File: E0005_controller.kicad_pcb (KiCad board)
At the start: 4 copper layers, 125 x 73 mm, 270 parts, among them J1 SM04B-GHS-TB, J10 FH12-18S-0.5SH, J11 USB4105-GF-A, J12 SM02B-GHS-TB, J2 SM04B-GHS-TB, J3 SM04B-GHS-TB, J4 SM04B-GHS-TB, J5 SM06B-GHS-TB, J6 SM02B-GHS-TB, J7 SM02B-GHS-TB, J8 SM02B-GHS-TB, J9 SM02B-GHS-TB, Q1 PSMN2R0-30YLDX, Q11 2N7002, Q12 2N7002, Q13 AO3401A, Q14 2N7002, Q2 PSMN2R0-30YLDX, Q3 2N7002, Q4 2N7002, Q5 2N7002, Q6 2N7002, Q7 2N7002, SW1 PWR, SW2 BOOT, SW3 RESET, U1 ESP32-S3-WROOM-1-N16R2, U10 TPS259470ARPW, U11 TPS259470ARPW, U12 TPS259470ARPW, U13 TPS259470ARPW, U14 TPS259470ARPW, U15 MAX17205G+, U16 TPS259470ARPW, U17 TPS56637RPAR, U2 BQ25887RGER, U4 USBLC6-2SC6, U5 TPS629210DRL, U6 S-8252AAG-M6T1U, U8 PCA9548APW, U9 TCA9535PWR

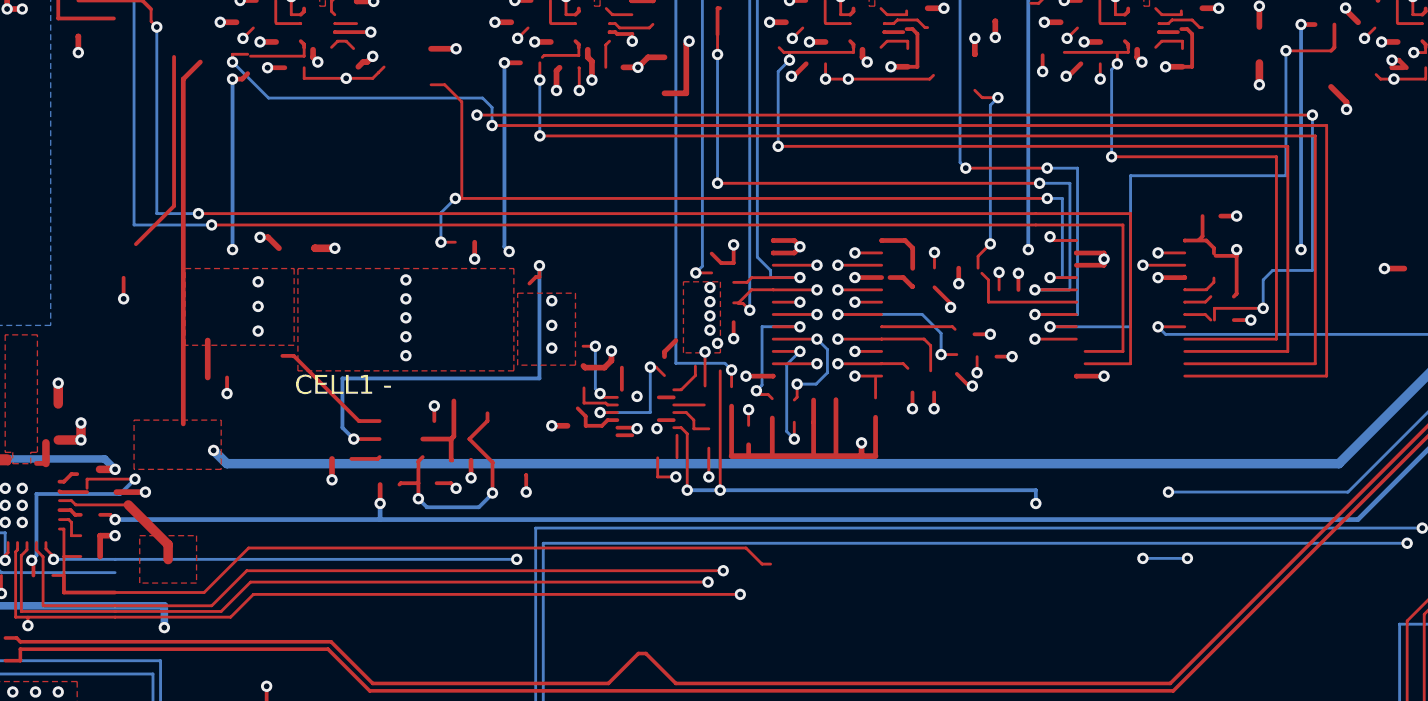
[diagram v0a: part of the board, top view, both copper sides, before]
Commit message: E0005 routing: CHG_PG_N and BUCK_PG from U9 to the west power stage (band / west corridor; centre B lane + In2), R92.1 own 3V3 via, BUCK_PG pin link hugs U9
Co-Authored-By: Claude Opus 5.5 <noreply@anthropic.com>
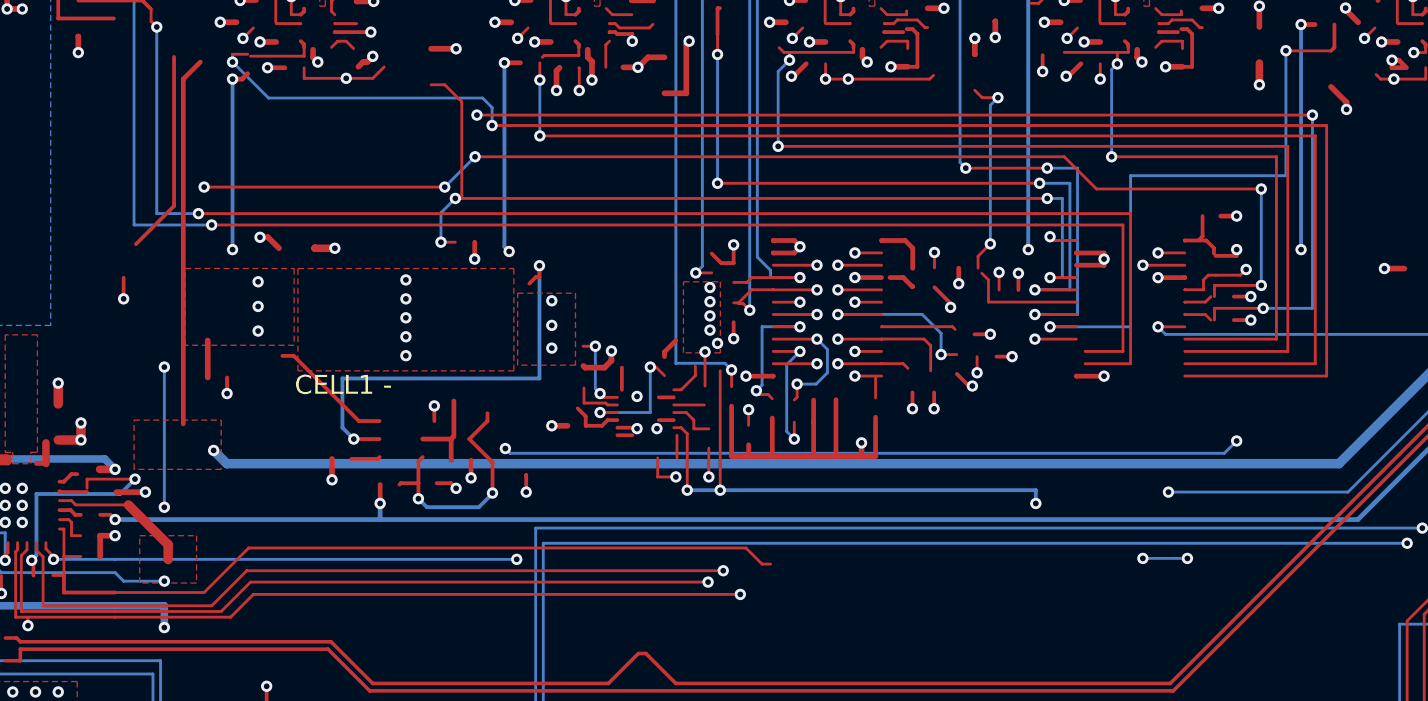
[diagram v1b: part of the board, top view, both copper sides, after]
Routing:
- net BUCK_PG: track 6.88 -> 111.0 mm, vias 1 -> 4
- net CHG_PG_N: track 9.65 -> 99.4 mm, vias 1 -> 9
- net +3V3: track 172.1 -> 170.8 mm, vias 41 -> 42

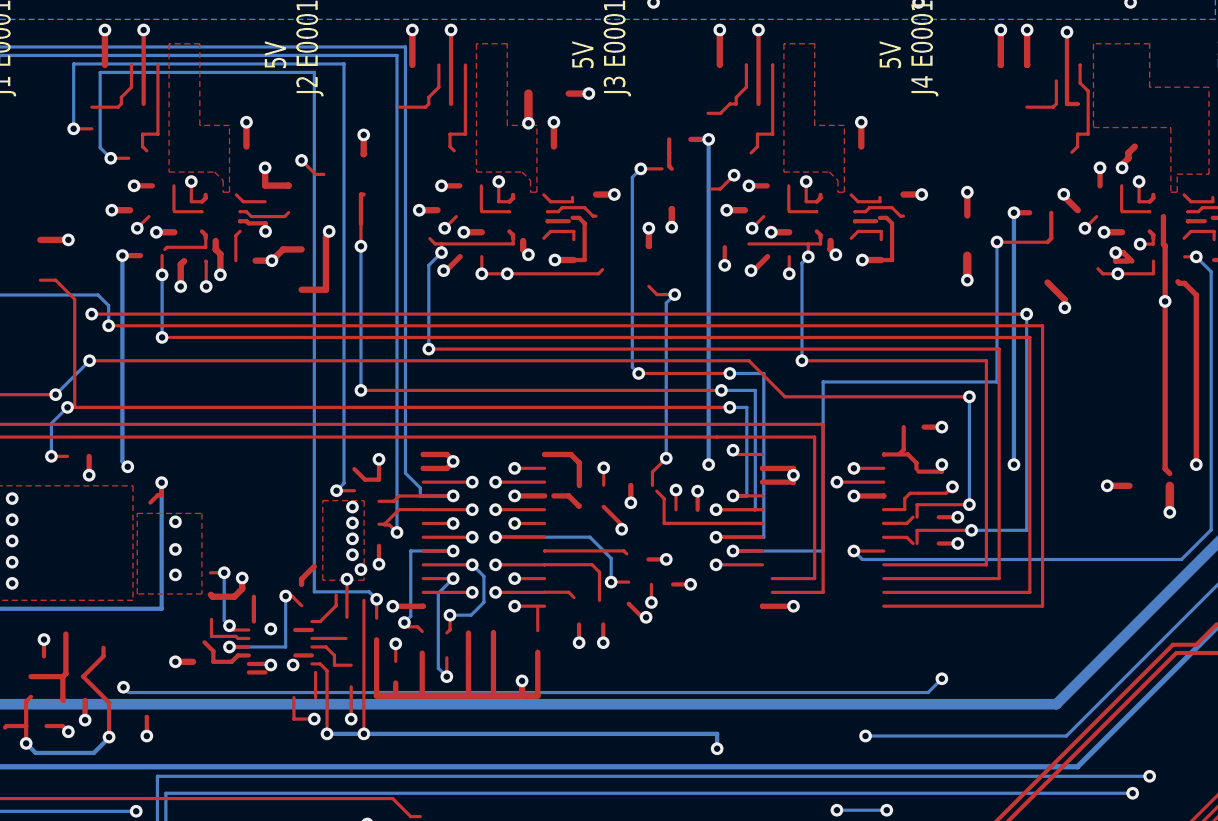
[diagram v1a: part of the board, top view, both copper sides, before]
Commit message: E0005 routing: PORT5_SCL/SDA U8 -> south B lanes -> F columns -> port 5 pull-ups; Q7.2 GND via, BUCK_PG via shift; probe resolves pads in the final frame
Co-Authored-By: Claude Opus 5.5 <noreply@anthropic.com>
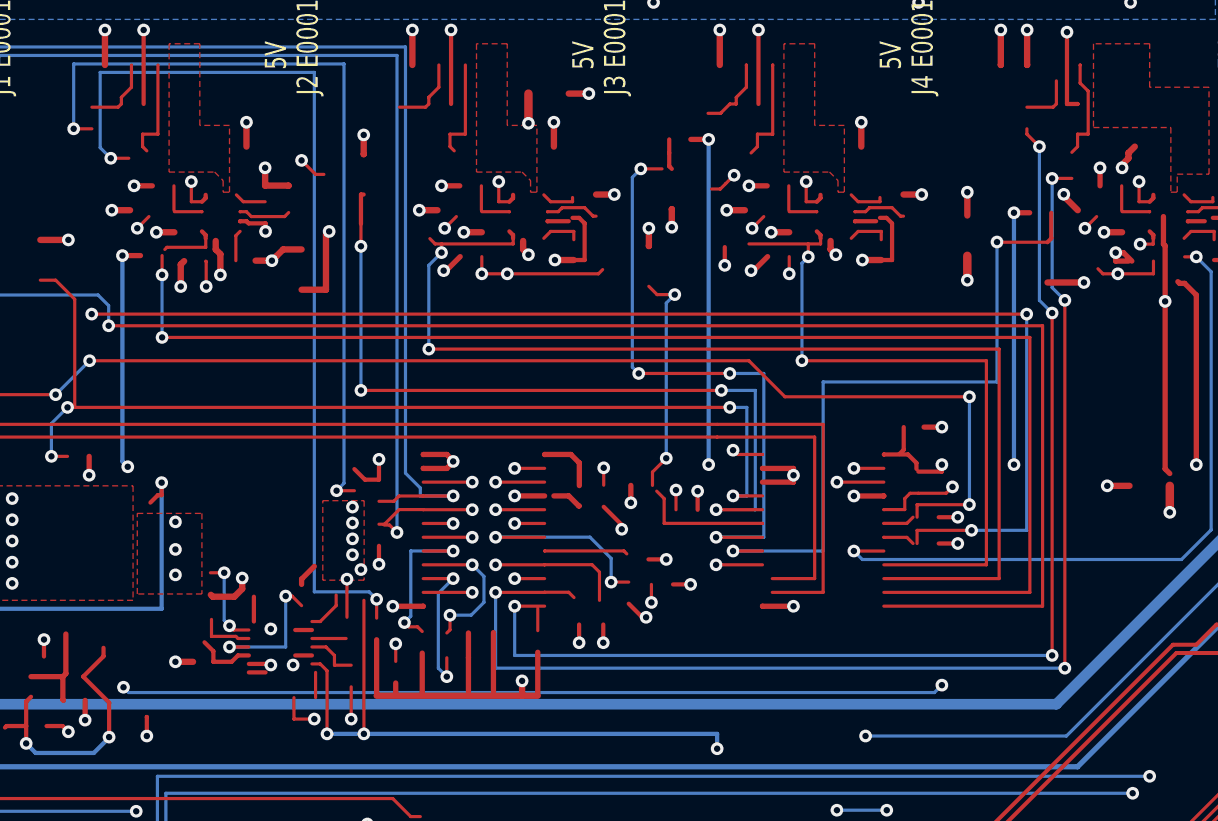
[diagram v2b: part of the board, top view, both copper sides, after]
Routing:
- net /I2C mux, expander, 5 V peripheral ports/PORT5_SCL: track 3.81 -> 58.5 mm, vias 1 -> 4
- net /I2C mux, expander, 5 V peripheral ports/PORT5_SDA: track 2.44 -> 55.5 mm, vias 1 -> 4

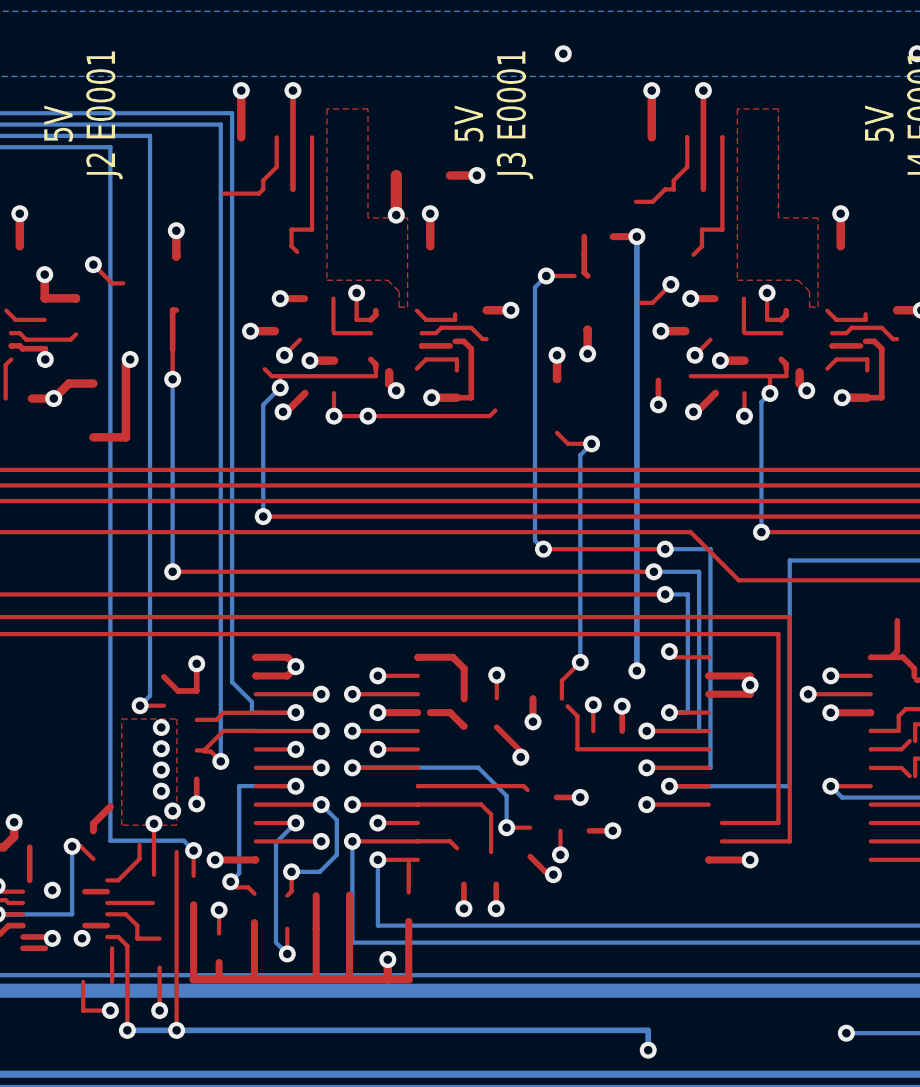
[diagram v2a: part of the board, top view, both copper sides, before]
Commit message: E0005 routing: PORT3/4 SCL/SDA through U8 channels and band B columns to the port pull-ups, MUX6_SCL link on In2, R64.1 3V3 via moved
Co-Authored-By: Claude Opus 5.5 <noreply@anthropic.com>
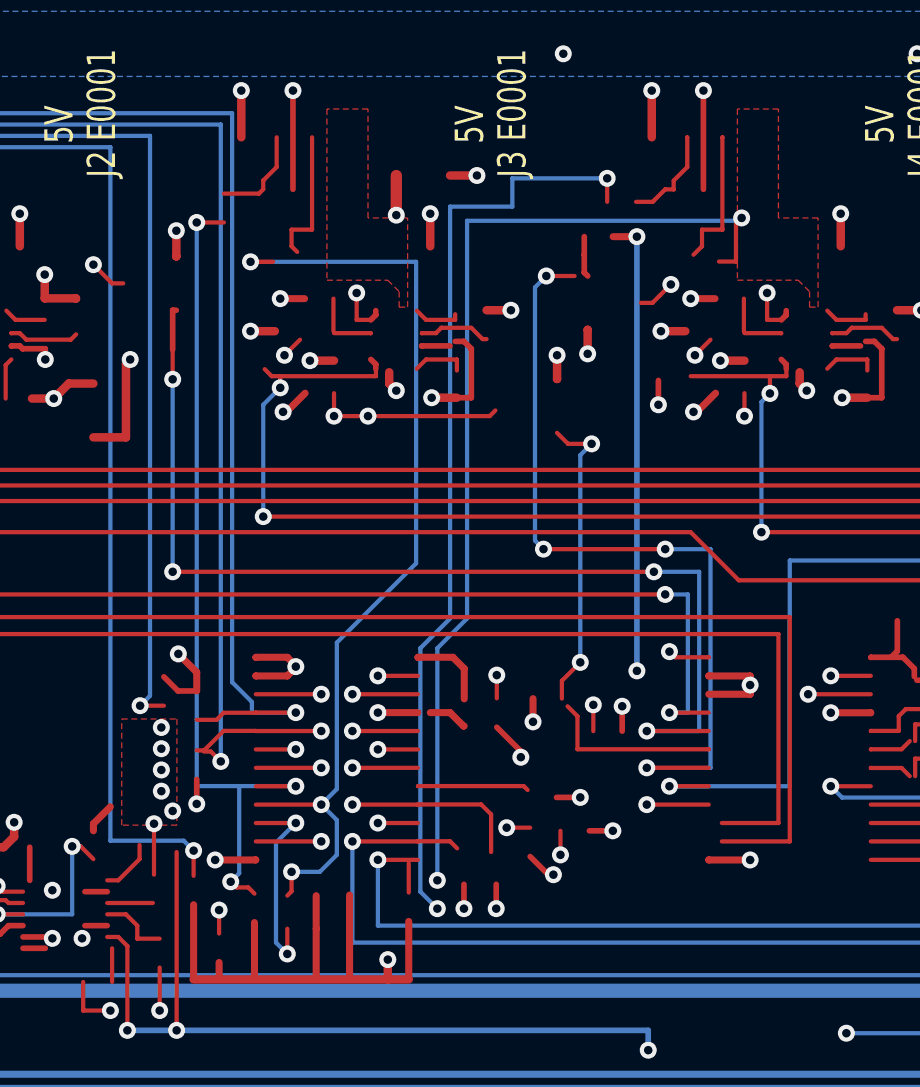
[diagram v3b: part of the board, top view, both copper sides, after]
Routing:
- net /I2C mux, expander, 5 V peripheral ports/PORT4_SCL: track 9.00 -> 48.8 mm, vias 2 -> 4
- net /I2C mux, expander, 5 V peripheral ports/PORT4_SDA: track 7.39 -> 46.5 mm, vias 2 -> 4
- net /I2C mux, expander, 5 V peripheral ports/PORT3_SCL: track 7.07 -> 34.3 mm, vias 2 -> 3
- net /I2C mux, expander, 5 V peripheral ports/PORT3_SDA: track 7.93 -> 30.3 mm, vias 2 -> 3
- net +3V3: track 170.8 -> 171.5 mm

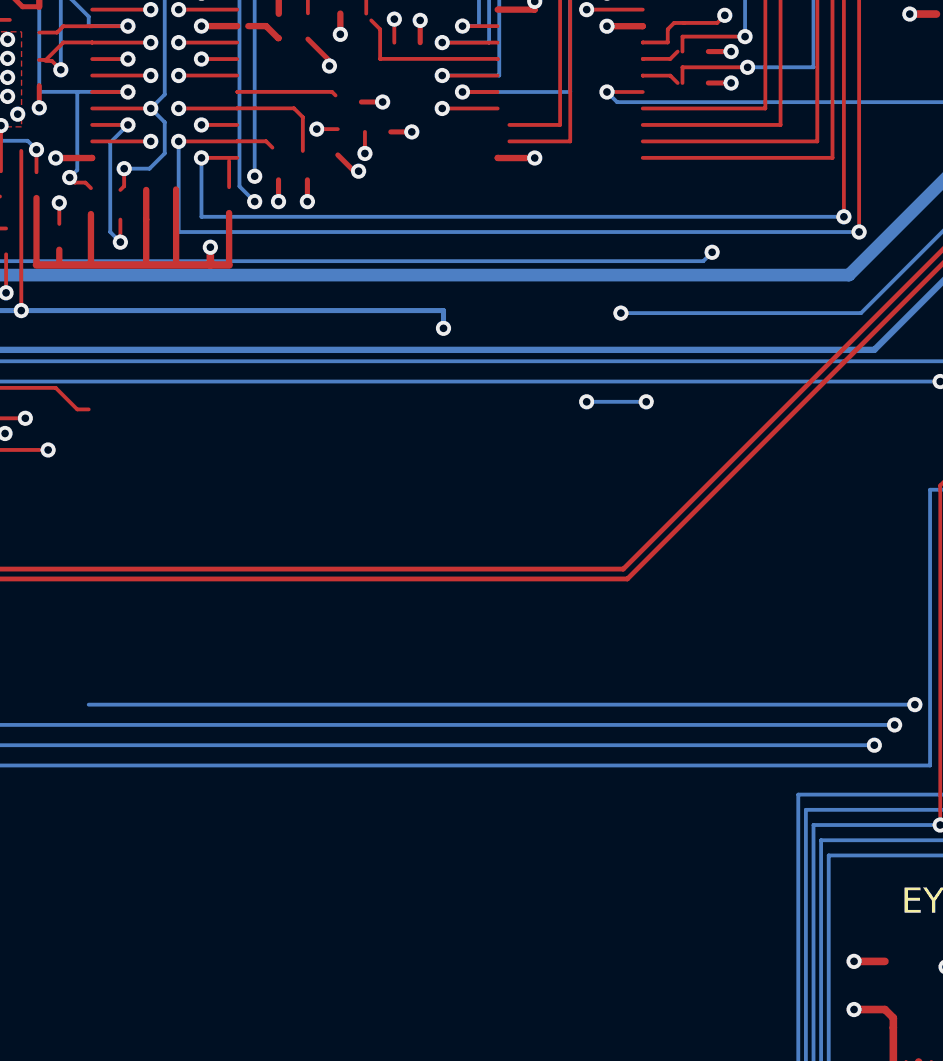
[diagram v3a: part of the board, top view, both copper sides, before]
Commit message: E0005 routing: LCD_SCL/SDA U8 -> J10 (In2 columns, B under USB, F diagonals), PORT4/PORT3_SCL/LCD vias, 3V3 rail via moved
Co-Authored-By: Claude Opus 5.5 <noreply@anthropic.com>
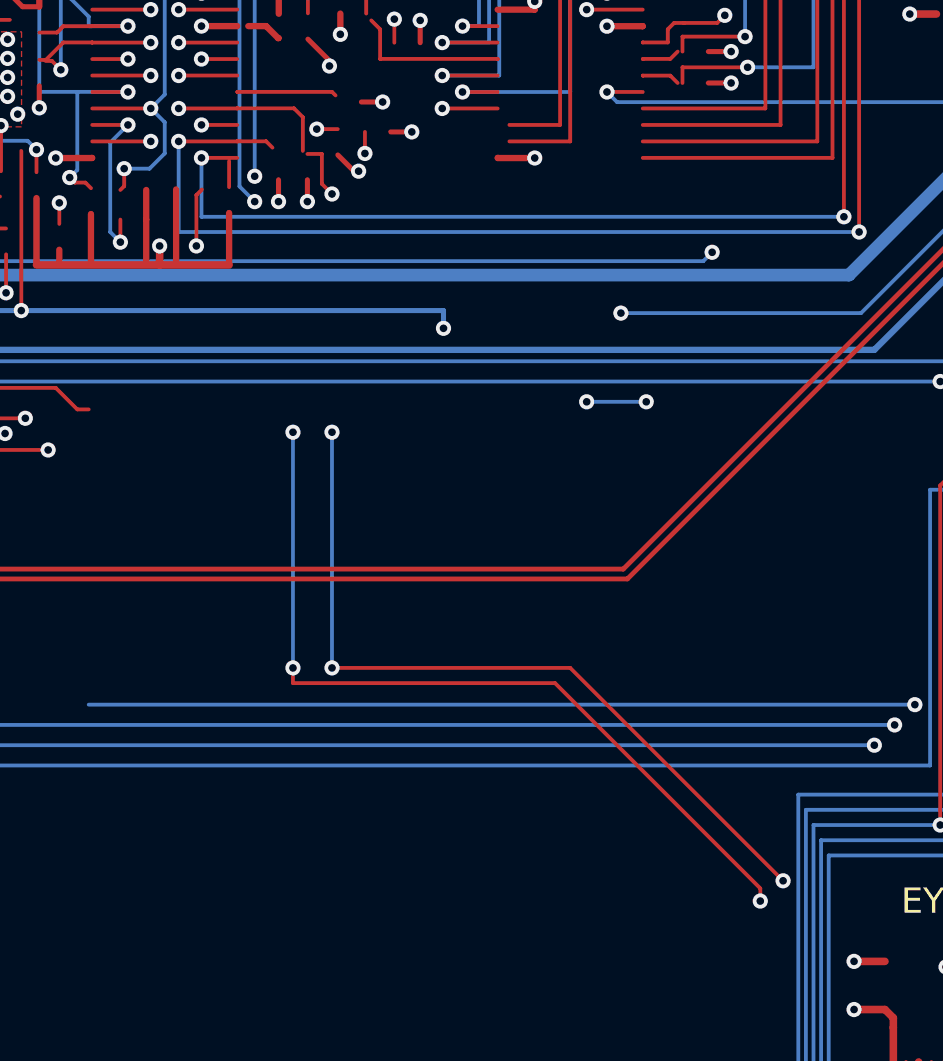
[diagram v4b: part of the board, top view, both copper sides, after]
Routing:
- net LCD_SDA: track 24.0 -> 78.7 mm, vias 2 -> 6
- net LCD_SCL: track 27.6 -> 71.3 mm, vias 2 -> 6
